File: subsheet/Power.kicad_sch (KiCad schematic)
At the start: 27 parts, among them J501 Barrel_Jack, J502 PWR_IN, J503 ALTERNATE, Q501 DTC114E, Q502 DTC114E, U501 TPS2552DBV, U502 TPS2552DBV

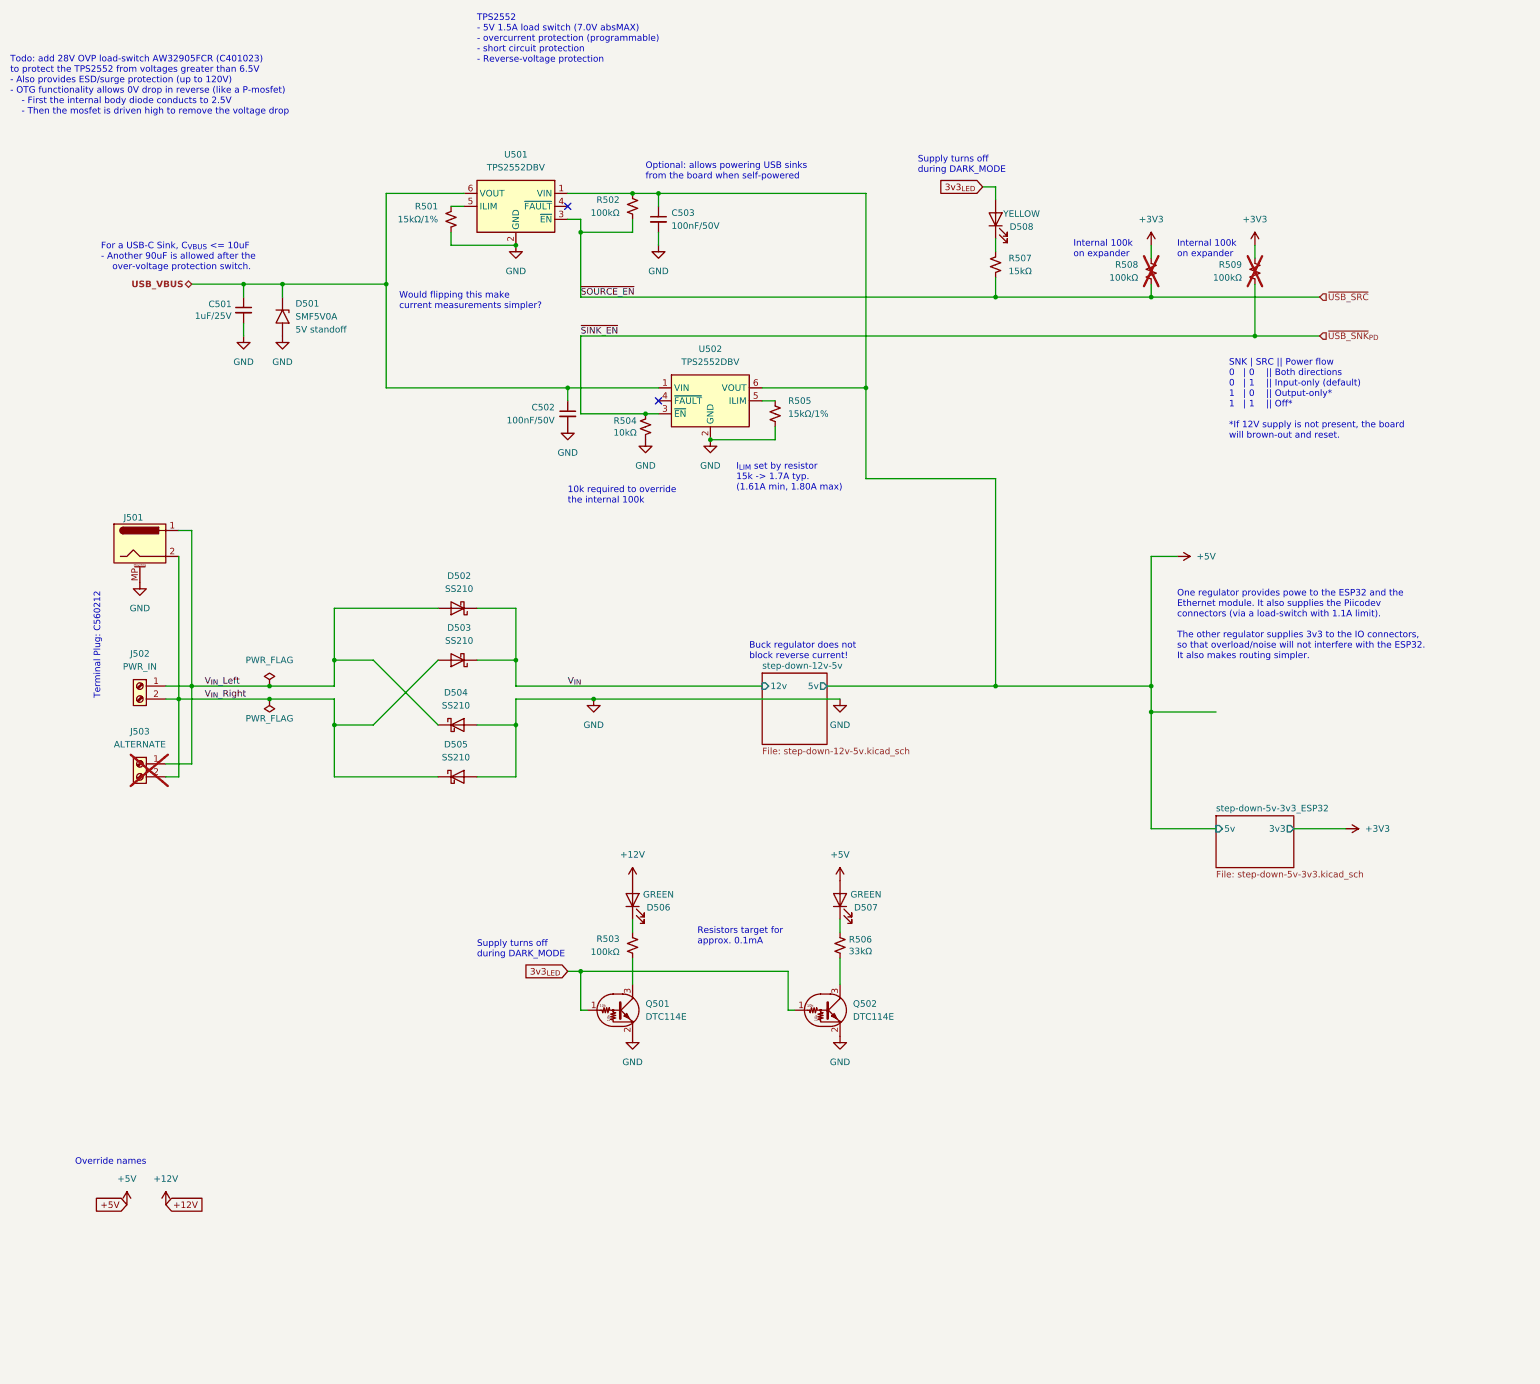
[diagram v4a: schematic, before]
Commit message: Apply XOR to 5V buck reg and USB power
Some 5V regulators will be very unhappy if a higher-voltage is applied -
e.g. from USB. Therefore, use a comparator to turn off the load-switch
when 12V power is present.

Circuit got a bit more complex because it needs to deal with dynamic
situations as things are plugged in. Will still need some work, likely.
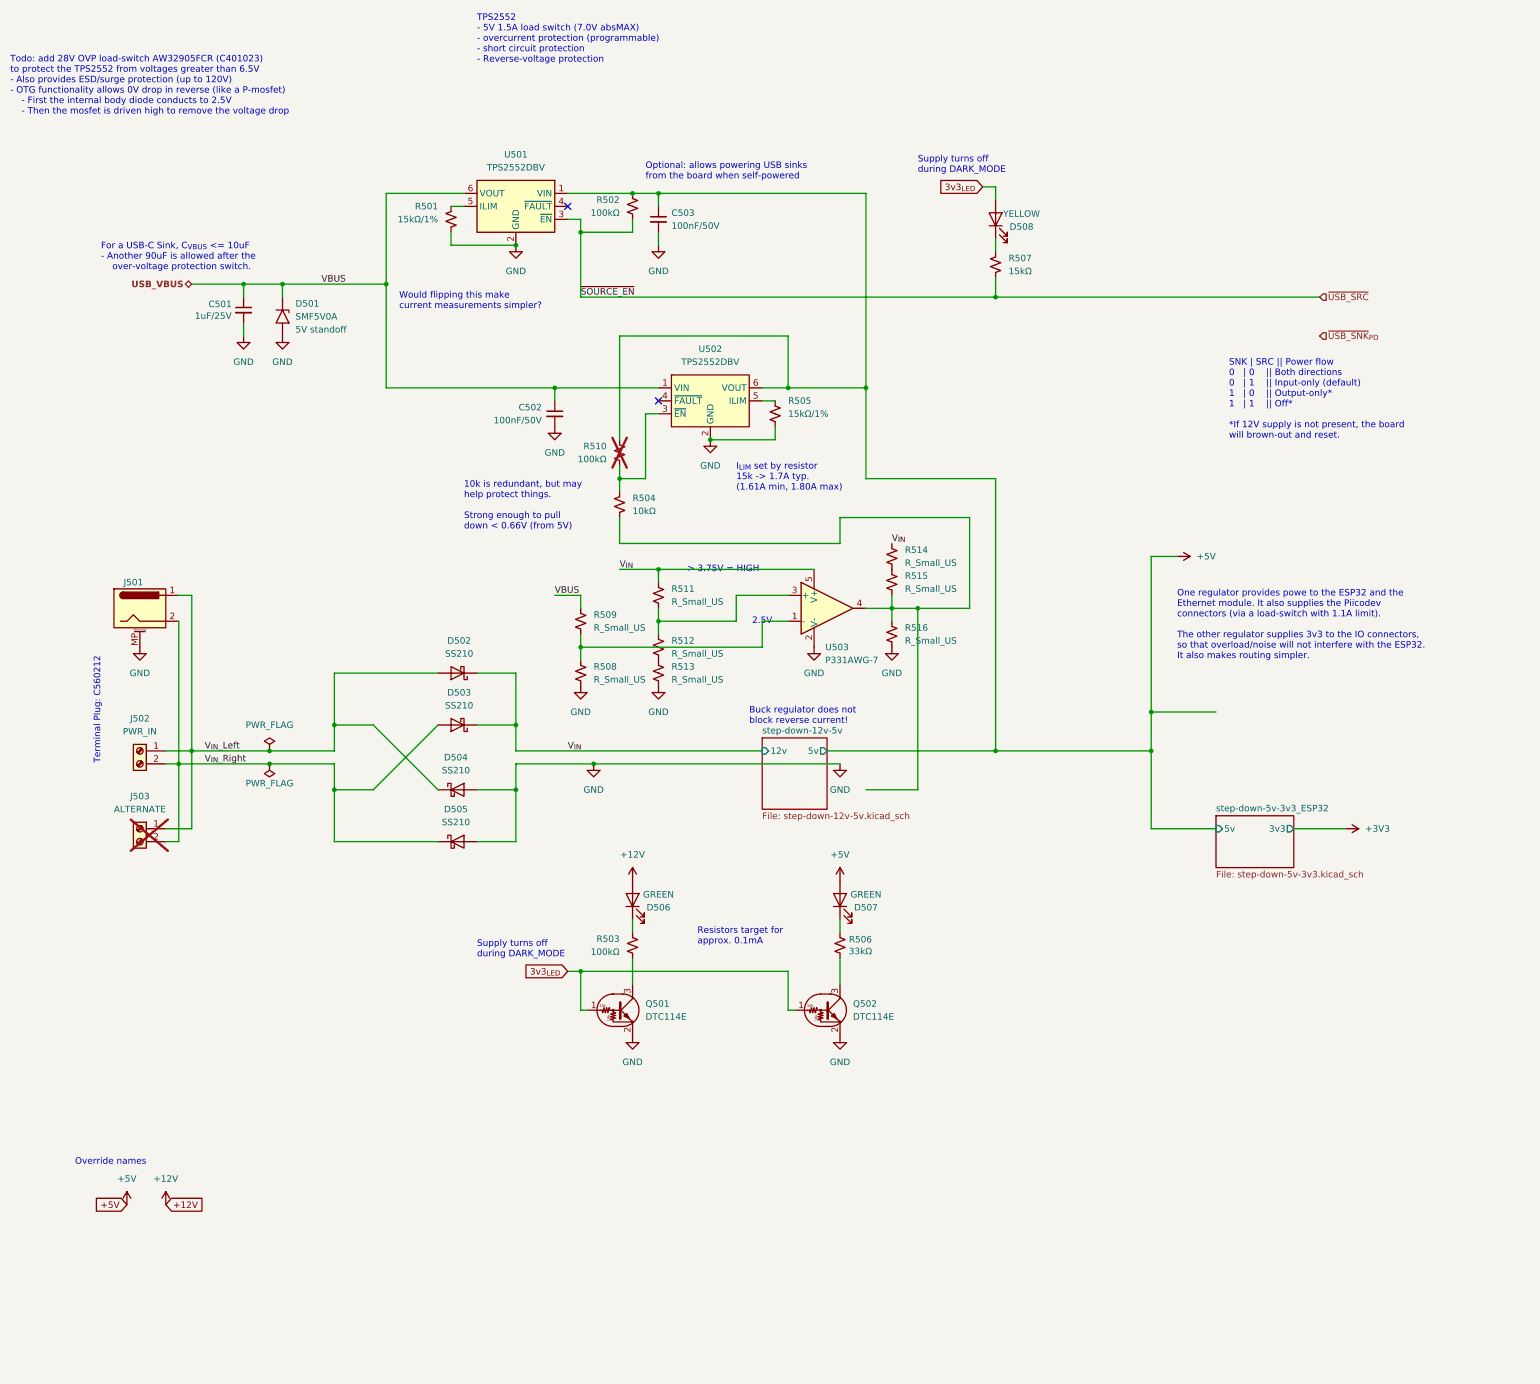
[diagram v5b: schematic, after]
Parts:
- added R510: 100kΩ, Resistor_SMD:R_0603_1608Metric, symbol Device:R_Small_US
- added R511, R512, R513, R514, R515, R516: R_Small_US, symbol Device:R_Small_US
- added U503: P331AWG-7, Package_TO_SOT_SMD:SOT-23-5, symbol Comparator:TL331
- R508, R509: value 100kΩ -> R_Small_US; footprint Resistor_SMD:R_0603_1608Metric -> (none); LCSC C25803 -> (none); now fitted; now in the parts list
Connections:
- net +3V3: no longer R508.1, R509.1
- net +5V: now also R510.1
- net GND: now also R508.2, R513.2, R516.2, U503.2 (V-); no longer R504.2
- net USB_VBUS: now also R509.1
- net V_{IN}: now also R511.1, R514.1, U503.5 (V+)
- net ~{USB_SNK}_{PD}: no longer R504.1, R509.2, U502.3 (~{EN})
- net ~{USB_SRC}: no longer R508.2
- new net: R504.1, R510.2, U502.3 (~{EN})
- new net: R511.2, R512.1, U503.3 (+)
- new net: R512.2, R513.1
- new net: R508.1, R509.2, U503.1 (-)
- new net: R504.2, R515.2, R516.1, U503.4
- new net: R514.2, R515.1
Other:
- note added: "10k is redundant, but may help protect things. Strong enough to pull down < 0.66V (from 5V)"
- note added: "2.5V"
- note added: "> 3.75V = HIGH"
- note removed: "10k required to override the internal 100k"
- note removed: "Internal 100k on expander"
- moved on the sheet: C502, D502, D503, D504, D505, J501, J502, J503, R504

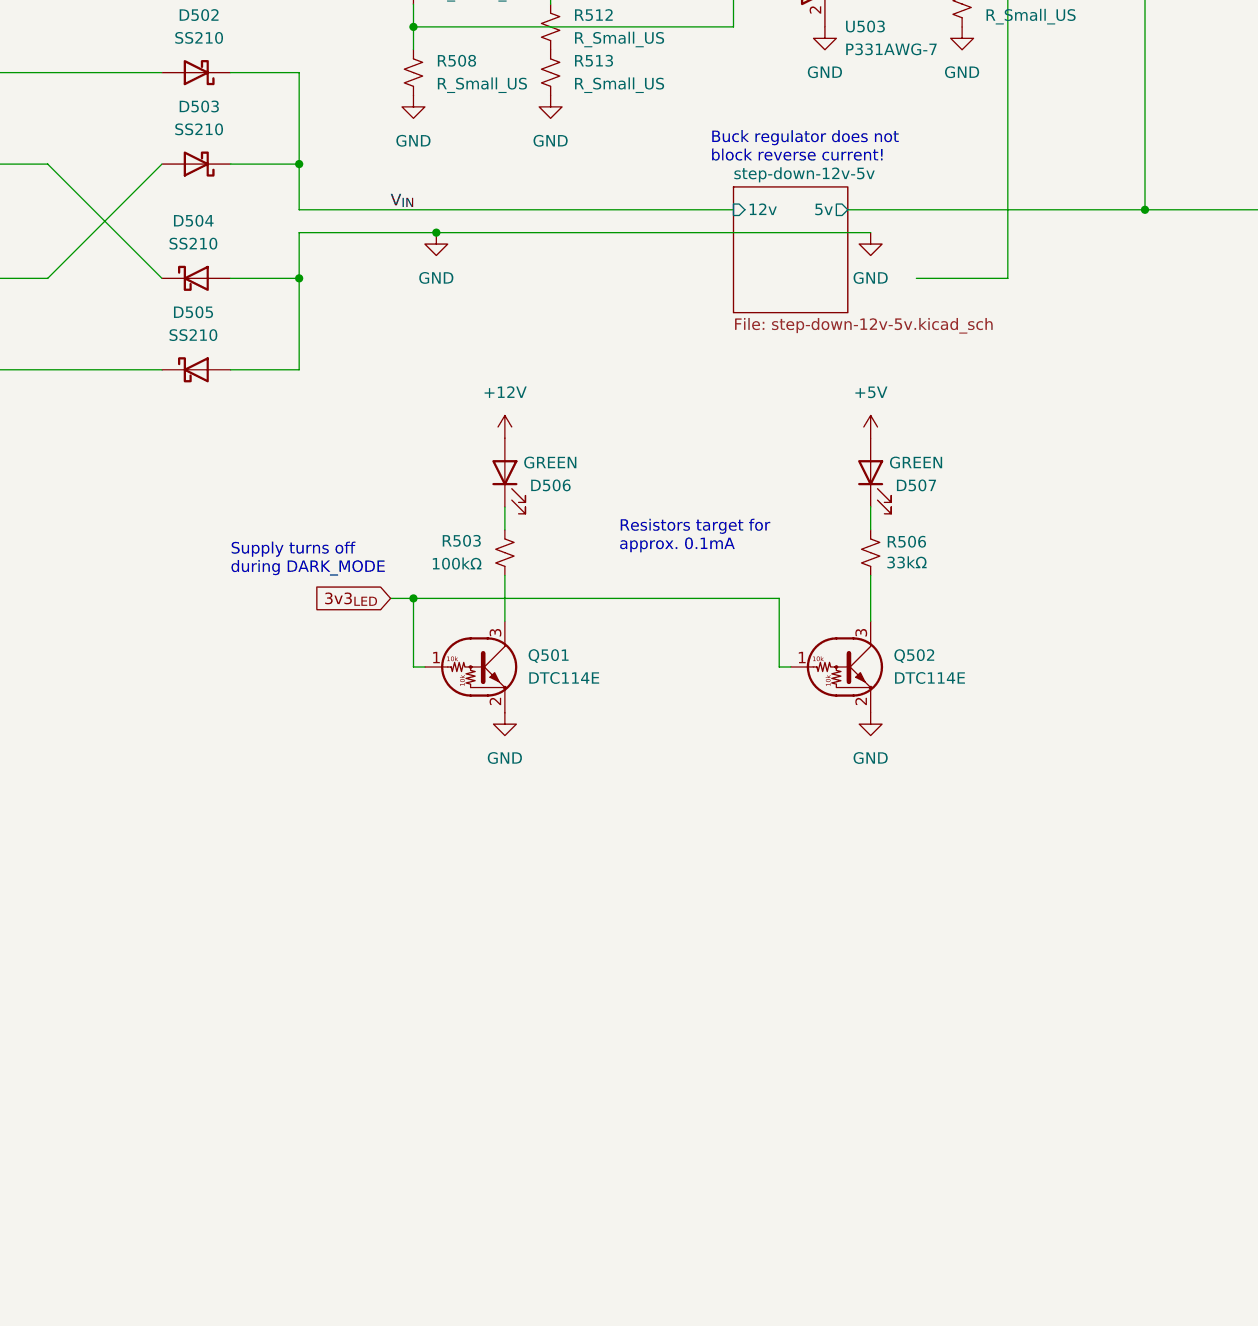
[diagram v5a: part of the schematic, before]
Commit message: Replace buck-regulator with buck-boost regulator
Replaced the buck-regulator with a buck-boost regulator. The primary
purpose is because the buck-regulator could fail when a higher-voltage
output was conected. The buck-regulators internal switches and design
should be much less vulnerable for this.

A second benefit of the buck-boost regulator is thata 5V input can now
still be used, as it accounts for the voltage-drop from the
bridge-rectifier diodes.
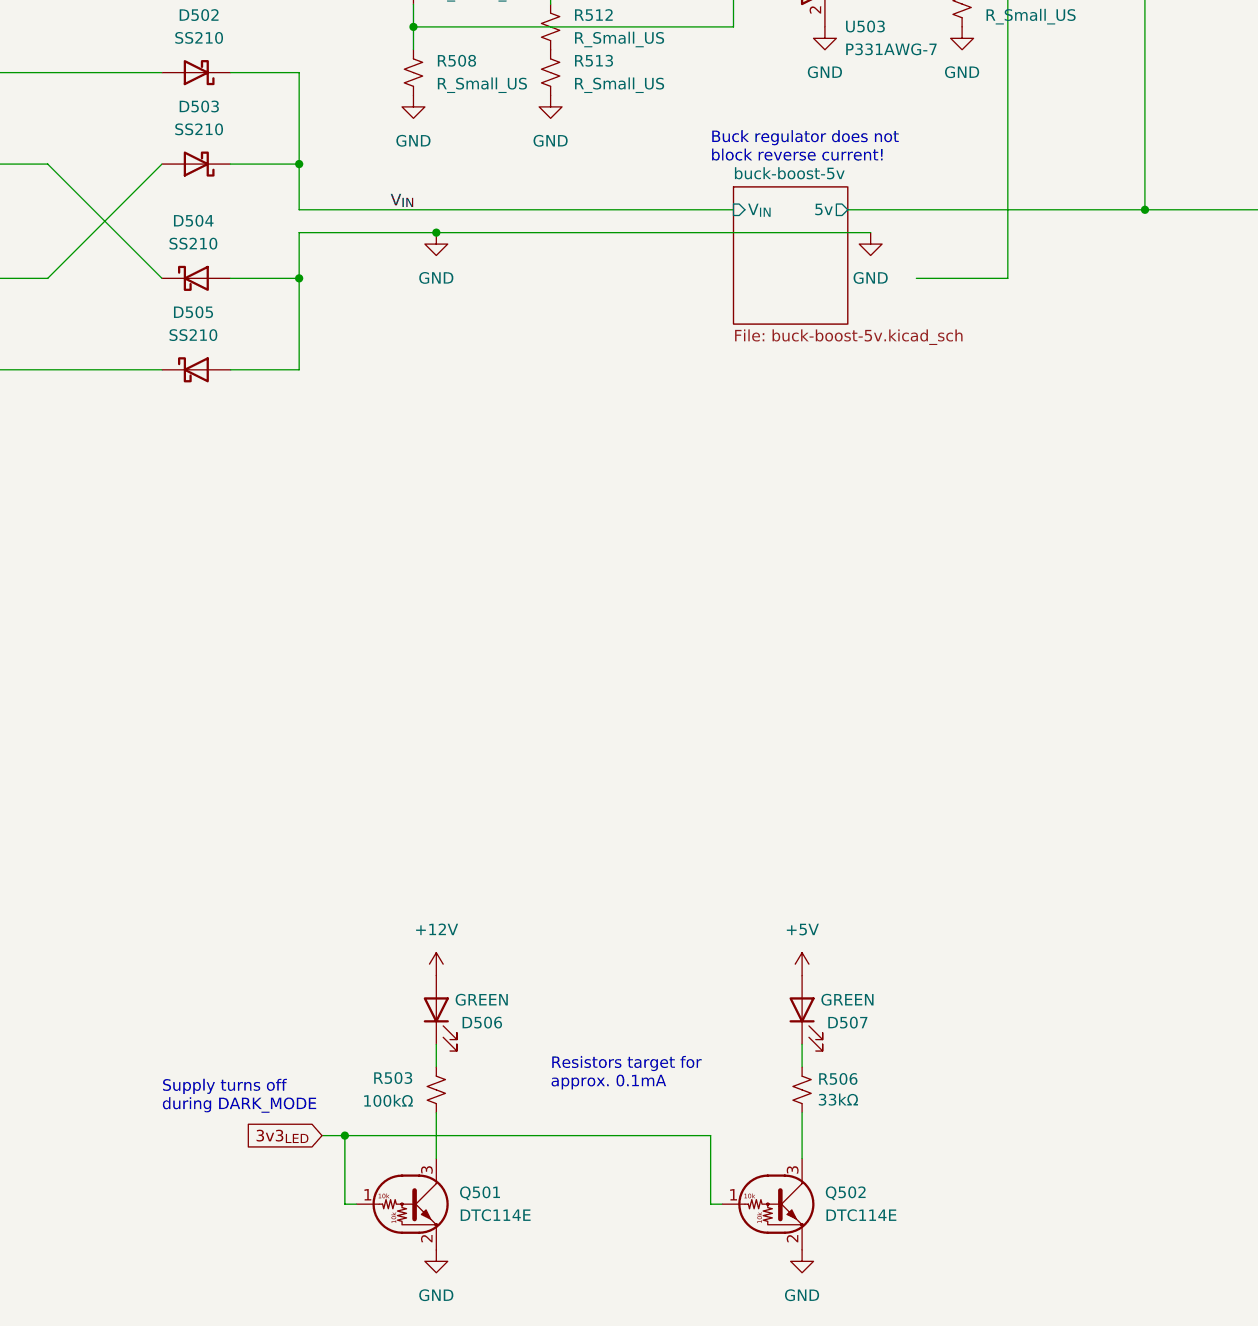
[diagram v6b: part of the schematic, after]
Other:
- removed sheet step-down-12v-5v
- added sheet buck-boost-5v (buck-boost-5v.kicad_sch)
- moved on the sheet: D506, D507, Q501, Q502, R503, R506
